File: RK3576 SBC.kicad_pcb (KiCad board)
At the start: 2 copper layers, 2.2 x 8.1 mm, 692 parts, among them J1 Conn_01x04_Pin, J10 DSI Connector, J11 1-2199230-5, J12 Raspberry_Pi_4, J13 JST_03, J15 Conn_02x10_Counter_Clockwise, J16 Conn_ARM_SWD_TagConnect_TC203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, J17 TE_2199230-3, J3 USB3_A_Stacked, J4 USB3_A_Stacked, J5 POE Connector, J7 HDMI_A, J8 Micro_SD_Card_Det1, J9 CSI Connector, Q1 2SK3018, Q2 2SK3018, Q3 2SK3018, Q4 2SK3018, Q5 2SK3018, Q6 2SK3018, Q7 AO3401A, SW1 SW_Push, SW3 SW_Push, SW4 SW_Push, SW5 SW_Push, SW6 SW_Push, U1 MAX14713EWL+T, U13 TPD4E05U06DQA, U14 TPD4E05U06DQA, U15 TPD4E05U06DQA, U16 TPD4E05U06DQA, U17 RTS5411S-GR, U18 MT62F1G32D4DR-031, U19 RTL8211F-CG, U2 RK806S-5, U21 TXB0104PW, U22 TPD4E05U06DQA, U23 TPD4E05U06DQA, U24 TPD4E05U06DQA, U25 HN8T05DEHK-X073, U26 TLV75801PDBV, U28 TPD4E05U06DQA, U29 TPD4E05U06DQA, U3 RK3576, U30 BGS12P2L6E6327XTSA1, U32 RV-3028-C7, U33 ETA7014S2G, U34 RP2350A, U35 W25Q128JVS, U36 0.96 OLED Display 8 pins, U4 ETA7014S2G, U5 FUSB302BMPX, U6 TPD4E05U06DQA, U7 TPD4E05U06DQA, U8 TPD4E05U06DQA, Y1 TXM24M0004322FBCDO00T, Y2 XTM32026000FT00351001, Y3 K3A120002010, Y4 SX32Y025000BC1T001, Y5 T3225374MDBDE2X, Y6 TAXM12M4RLBDDT2T

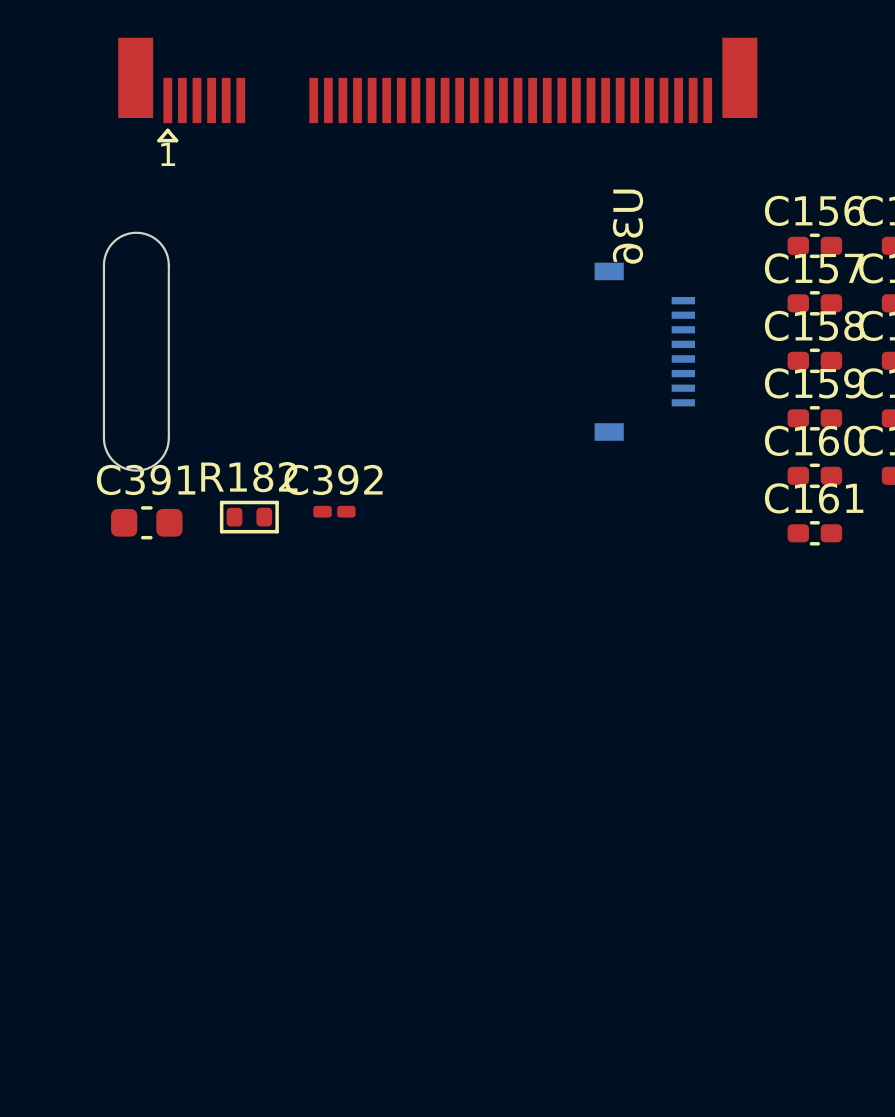
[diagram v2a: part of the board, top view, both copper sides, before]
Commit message: SBCv0.3
there is no big thing update just some LCSC & Mouser parts
and Big problem deleted alot of component values (:
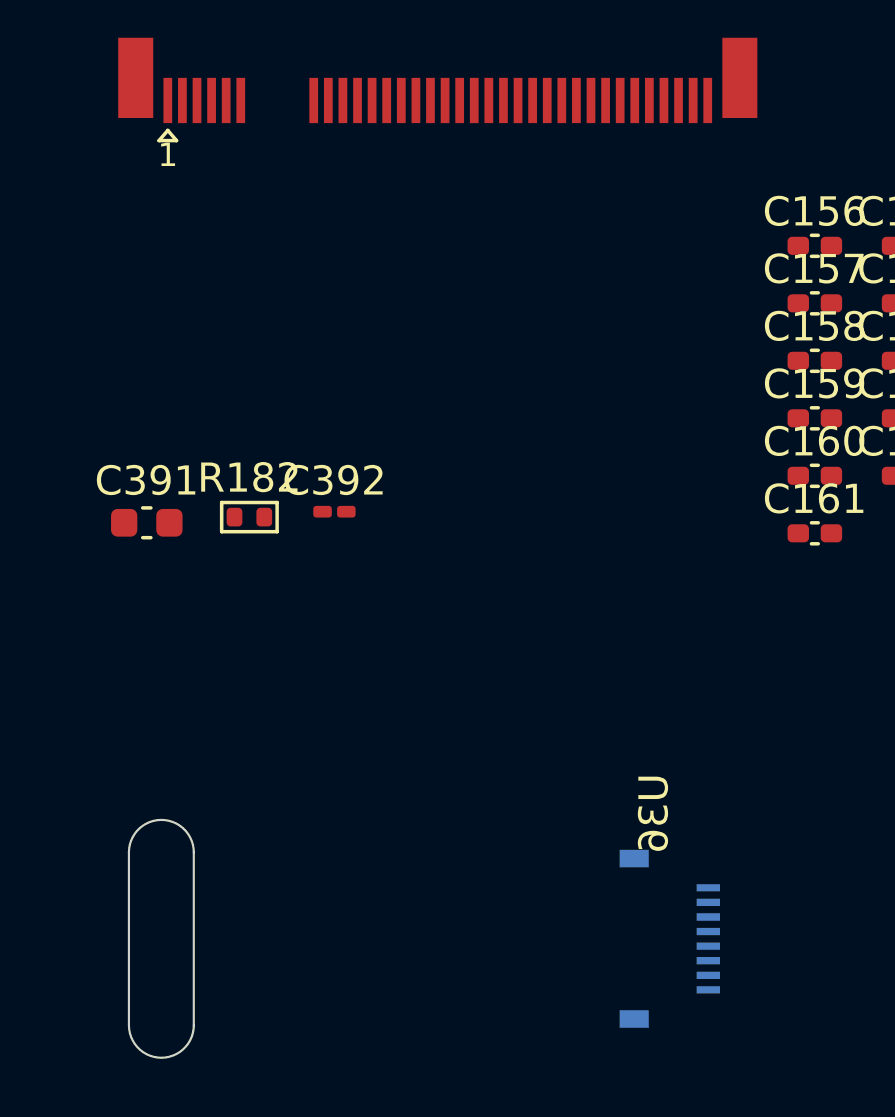
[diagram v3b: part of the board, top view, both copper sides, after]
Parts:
- moved U36 20.1 mm to (76.4, 184.6)
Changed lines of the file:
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@@
 	(footprint "Datasheet_Footprints:FFC-SMD_8P-P0.50_AFC42-S08FMA-1H_BOTTOM"
 		(layer "F.Cu")
-		(at 75.548393 164.431989)
+		(at 76.404197 184.55)
 		(descr "JUSHUO AFC42-S08FMA-1H FFC/FPC 8P 0.5mm bottom-contact R/A SMD, bottom-side mounting with FPC pass-through slot for 0.96in ST7735S display")
 		(property "Reference" "U36"
